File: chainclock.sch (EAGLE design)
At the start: 11 parts

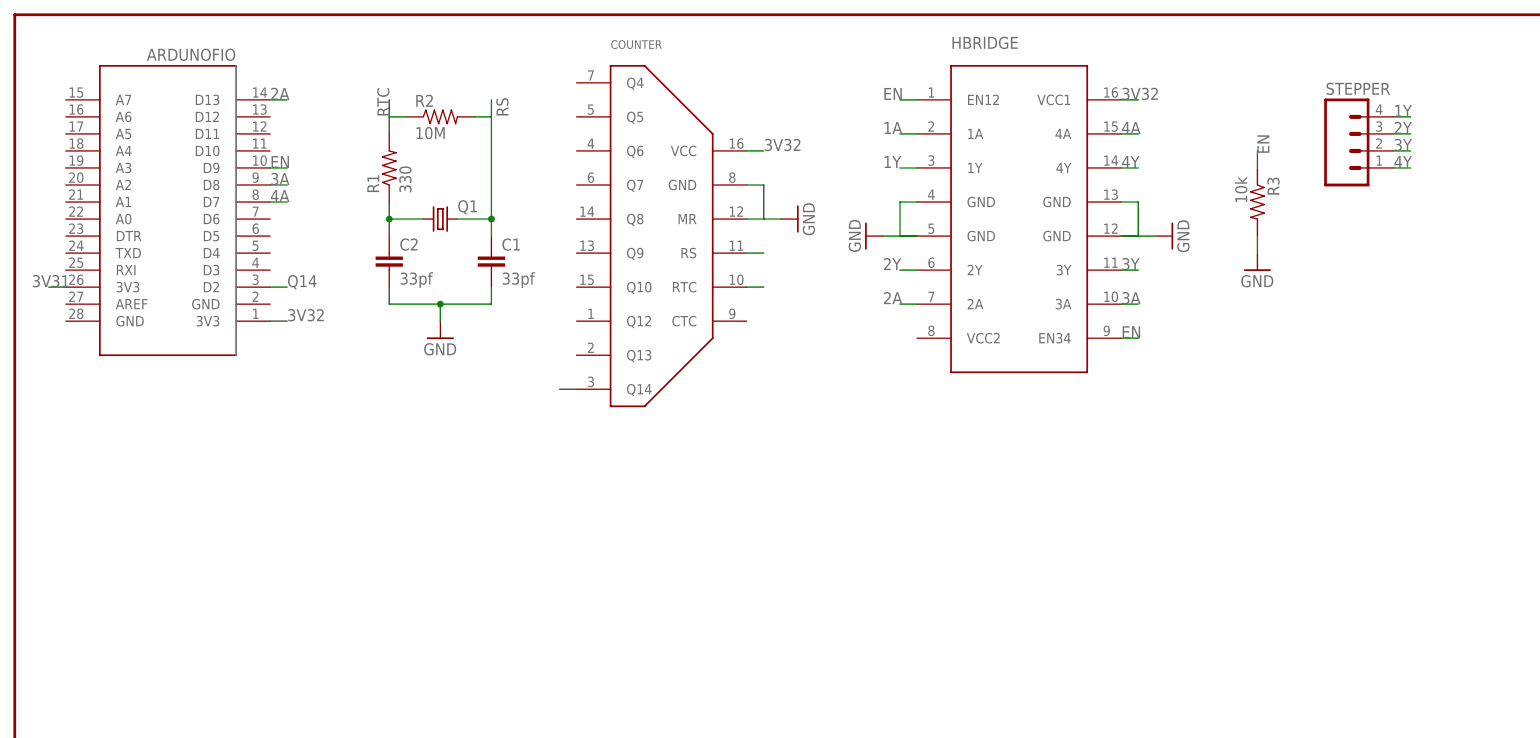
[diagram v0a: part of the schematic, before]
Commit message: Updates to chainclock, adding motor
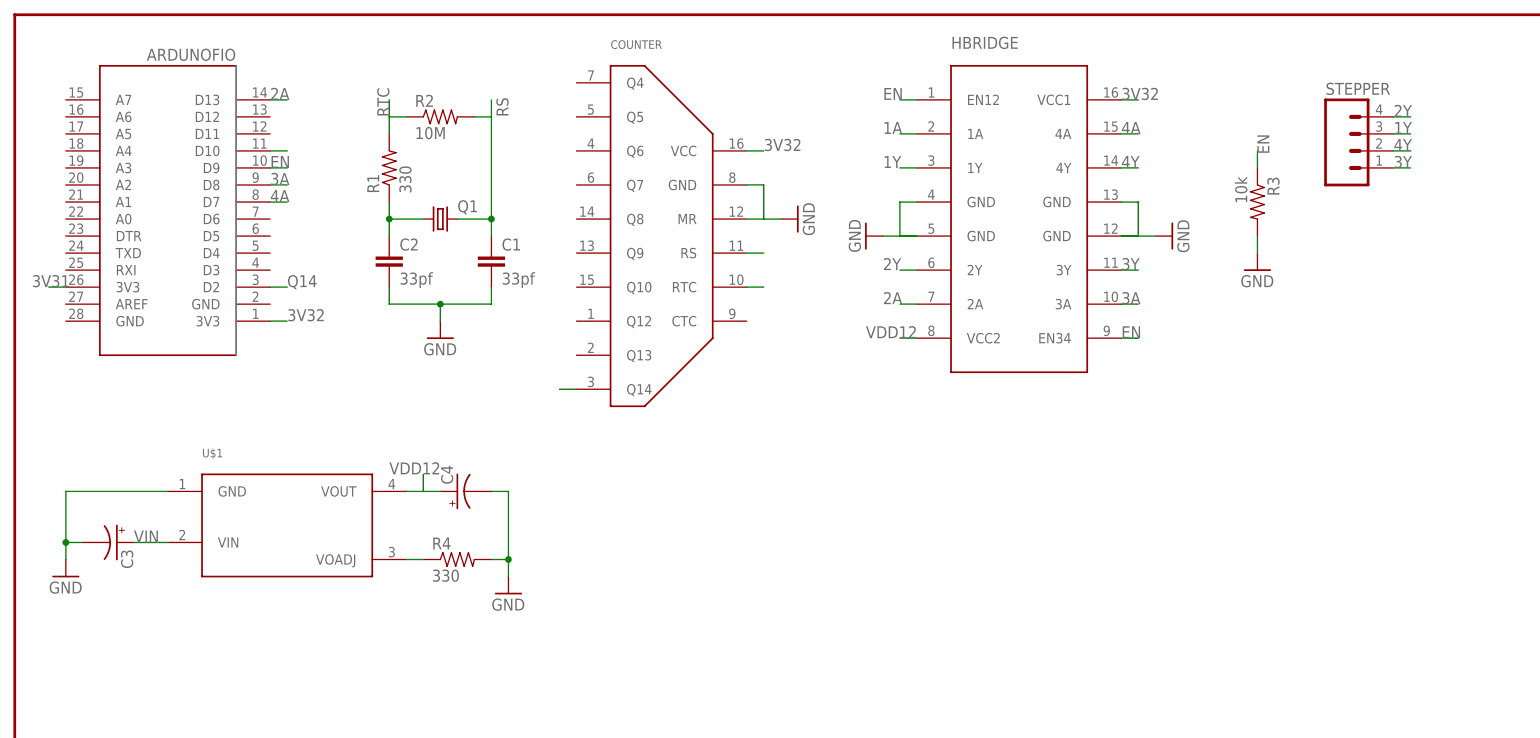
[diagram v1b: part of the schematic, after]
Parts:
- added C3, C4: (no value), SparkFun-Passives:CAP_POLPTH1
- added R4: 330, SparkFun-Resistors:RESISTOREZ
- added U$1: PTN0405C, desjardins:PTN0405C
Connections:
- new net N$3: R4.1, U$1.VOADJ
- new net VDD12: C4.+, HBRIDGE.VCC2, U$1.VOUT
- new net VIN: C3.+, U$1.VIN
- net 1A: now also ARDUNOFIO.D10
- net 1Y: now also STEPPER.3; no longer STEPPER.4
- net 2Y: now also STEPPER.4; no longer STEPPER.3
- net 3Y: now also STEPPER.1; no longer STEPPER.2
- net 4Y: now also STEPPER.2; no longer STEPPER.1
- net GND: now also C3.-, C4.-, R4.2, U$1.GND
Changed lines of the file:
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@@
 <layer number="97" name="Info" color="7" fill="1" visible="yes" active="yes"/>
 <layer number="98" name="Guide" color="6" fill="1" visible="yes" active="yes"/>
+<layer number="99" name="SpiceOrder" color="5" fill="1" visible="yes" active="yes"/>
 <layer number="100" name="Muster" color="7" fill="1" visible="no" active="no"/>
 <layer number="101" name="Patch_Top" color="12" fill="4" visible="yes" active="yes"/>
@@
 <part name="R3" library="SparkFun-Resistors" deviceset="RESISTOR" device="EZ" value="10k"/>
 <part name="GND5" library="SparkFun-Aesthetics" deviceset="GND" device=""/>
+<part name="U$1" library="desjardins" deviceset="PTN0405C" device=""/>
+<part name="C3" library="SparkFun-Passives" deviceset="CAP_POL" device="PTH1"/>
+<part name="C4" library="SparkFun-Passives" deviceset="CAP_POL" device="PTH1"/>
+<part name="GND6" library="SparkFun-Aesthetics" deviceset="GND" device=""/>
+<part name="R4" library="SparkFun-Resistors" deviceset="RESISTOR" device="EZ" value="330"/>
+<part name="GND8" library="SparkFun-Aesthetics" deviceset="GND" device=""/>
 </parts>
 <sheets>
@@
 <instance part="R3" gate="G$1" x="185.42" y="157.48" rot="R270"/>
 <instance part="GND5" gate="1" x="185.42" y="147.32"/>
+<instance part="U$1" gate="G$1" x="40.64" y="109.22"/>
+<instance part="C3" gate="G$1" x="15.24" y="106.68" rot="R270"/>
+<instance part="C4" gate="G$1" x="66.04" y="114.3" rot="R90"/>
+<instance part="GND6" gate="1" x="7.62" y="101.6"/>
+<instance part="R4" gate="G$1" x="66.04" y="104.14"/>
+<instance part="GND8" gate="1" x="73.66" y="99.06"/>
 </instances>
 <busses>
@@
 <wire x1="185.42" y1="152.4" x2="185.42" y2="149.86" width="0.1524" layer="91"/>
 <pinref part="GND5" gate="1" pin="GND"/>
+</segment>
+<segment>
+<pinref part="U$1" gate="G$1" pin="GND"/>
+<wire x1="22.86" y1="114.3" x2="7.62" y2="114.3" width="0.1524" layer="91"/>
+<wire x1="7.62" y1="114.3" x2="7.62" y2="106.68" width="0.1524" layer="91"/>
+<pinref part="C3" gate="G$1" pin="-"/>
+<wire x1="7.62" y1="106.68" x2="7.62" y2="104.14" width="0.1524" layer="91"/>
+<wire x1="10.16" y1="106.68" x2="7.62" y2="106.68" width="0.1524" layer="91"/>
+<junction x="7.62" y="106.68"/>
+<pinref part="GND6" gate="1" pin="GND"/>
+</segment>
+<segment>
+<pinref part="R4" gate="G$1" pin="2"/>
+<wire x1="71.12" y1="104.14" x2="73.66" y2="104.14" width="0.1524" layer="91"/>
+<wire x1="73.66" y1="104.14" x2="73.66" y2="101.6" width="0.1524" layer="91"/>
+<pinref part="GND8" gate="1" pin="GND"/>
+<pinref part="C4" gate="G$1" pin="-"/>
+<wire x1="71.12" y1="114.3" x2="73.66" y2="114.3" width="0.1524" layer="91"/>
+<wire x1="73.66" y1="114.3" x2="73.66" y2="104.14" width="0.1524" layer="91"/>
+<junction x="73.66" y="104.14"/>
 </segment>
 </net>
@@
 <label x="129.54" y="167.64" size="1.778" layer="95"/>
 </segment>
+<segment>
+<pinref part="ARDUNOFIO" gate="G$1" pin="D10"/>
+<wire x1="38.1" y1="165.1" x2="40.64" y2="165.1" width="0.1524" layer="91"/>
+</segment>
 </net>
 <net name="1Y" class="0">
@@
 </segment>
 <segment>
+<pinref part="STEPPER" gate="G$1" pin="3"/>
+<wire x1="205.74" y1="167.64" x2="208.28" y2="167.64" width="0.1524" layer="91"/>
+<label x="205.74" y="167.64" size="1.778" layer="95"/>
+</segment>
+</net>
+<net name="4A" class="0">
+<segment>
+<pinref part="HBRIDGE" gate="G$1" pin="4A"/>
+<wire x1="165.1" y1="167.64" x2="167.64" y2="167.64" width="0.1524" layer="91"/>
+<label x="165.1" y="167.64" size="1.778" layer="95"/>
+</segment>
+<segment>
+<pinref part="ARDUNOFIO" gate="G$1" pin="D7"/>
+<wire x1="38.1" y1="157.48" x2="40.64" y2="157.48" width="0.1524" layer="91"/>
+<label x="38.1" y="157.48" size="1.778" layer="95"/>
+</segment>
+</net>
+<net name="4Y" class="0">
+<segment>
+<pinref part="HBRIDGE" gate="G$1" pin="4Y"/>
+<wire x1="165.1" y1="162.56" x2="167.64" y2="162.56" width="0.1524" layer="91"/>
+<label x="165.1" y="162.56" size="1.778" layer="95"/>
+</segment>
+<segment>
+<pinref part="STEPPER" gate="G$1" pin="2"/>
+<wire x1="205.74" y1="165.1" x2="208.28" y2="165.1" width="0.1524" layer="91"/>
+<label x="205.74" y="165.1" size="1.778" layer="95"/>
+</segment>
+</net>
+<net name="3Y" class="0">
+<segment>
+<pinref part="HBRIDGE" gate="G$1" pin="3Y"/>
+<wire x1="165.1" y1="147.32" x2="167.64" y2="147.32" width="0.1524" layer="91"/>
+<label x="165.1" y="147.32" size="1.778" layer="95"/>
+</segment>
+<segment>
+<pinref part="STEPPER" gate="G$1" pin="1"/>
+<wire x1="205.74" y1="162.56" x2="208.28" y2="162.56" width="0.1524" layer="91"/>
+<label x="205.74" y="162.56" size="1.778" layer="95"/>
+</segment>
+</net>
+<net name="3A" class="0">
+<segment>
+<pinref part="HBRIDGE" gate="G$1" pin="3A"/>
+<wire x1="165.1" y1="142.24" x2="167.64" y2="142.24" width="0.1524" layer="91"/>
+<label x="165.1" y="142.24" size="1.778" layer="95"/>
+</segment>
+<segment>
+<pinref part="ARDUNOFIO" gate="G$1" pin="D8"/>
+<wire x1="38.1" y1="160.02" x2="40.64" y2="160.02" width="0.1524" layer="91"/>
+<label x="38.1" y="160.02" size="1.778" layer="95"/>
+</segment>
+</net>
+<net name="2A" class="0">
+<segment>
+<pinref part="HBRIDGE" gate="G$1" pin="2A"/>
+<wire x1="134.62" y1="142.24" x2="132.08" y2="142.24" width="0.1524" layer="91"/>
+<label x="129.54" y="142.24" size="1.778" layer="95"/>
+</segment>
+<segment>
+<pinref part="ARDUNOFIO" gate="G$1" pin="D13"/>
+<wire x1="38.1" y1="172.72" x2="40.64" y2="172.72" width="0.1524" layer="91"/>
+<label x="38.1" y="172.72" size="1.778" layer="95"/>
+</segment>
+</net>
+<net name="2Y" class="0">
+<segment>
+<pinref part="HBRIDGE" gate="G$1" pin="2Y"/>
+<wire x1="134.62" y1="147.32" x2="132.08" y2="147.32" width="0.1524" layer="91"/>
+<label x="129.54" y="147.32" size="1.778" layer="95"/>
+</segment>
+<segment>
 <pinref part="STEPPER" gate="G$1" pin="4"/>
 <wire x1="205.74" y1="170.18" x2="208.28" y2="170.18" width="0.1524" layer="91"/>
@@
 </segment>
 </net>
-<net name="4A" class="0">
-<segment>
-<pinref part="HBRIDGE" gate="G$1" pin="4A"/>
-<wire x1="165.1" y1="167.64" x2="167.64" y2="167.64" width="0.1524" layer="91"/>
-<label x="165.1" y="167.64" size="1.778" layer="95"/>
-</segment>
-<segment>
-<pinref part="ARDUNOFIO" gate="G$1" pin="D7"/>
-<wire x1="38.1" y1="157.48" x2="40.64" y2="157.48" width="0.1524" layer="91"/>
-<label x="38.1" y="157.48" size="1.778" layer="95"/>
-</segment>
-</net>
-<net name="4Y" class="0">
-<segment>
-<pinref part="HBRIDGE" gate="G$1" pin="4Y"/>
-<wire x1="165.1" y1="162.56" x2="167.64" y2="162.56" width="0.1524" layer="91"/>
-<label x="165.1" y="162.56" size="1.778" layer="95"/>
-</segment>
-<segment>
-<pinref part="STEPPER" gate="G$1" pin="1"/>
-<wire x1="205.74" y1="162.56" x2="208.28" y2="162.56" width="0.1524" layer="91"/>
-<label x="205.74" y="162.56" size="1.778" layer="95"/>
-</segment>
-</net>
-<net name="3Y" class="0">
-<segment>
-<pinref part="HBRIDGE" gate="G$1" pin="3Y"/>
-<wire x1="165.1" y1="147.32" x2="167.64" y2="147.32" width="0.1524" layer="91"/>
-<label x="165.1" y="147.32" size="1.778" layer="95"/>
-</segment>
-<segment>
-<pinref part="STEPPER" gate="G$1" pin="2"/>
-<wire x1="205.74" y1="165.1" x2="208.28" y2="165.1" width="0.1524" layer="91"/>
-<label x="205.74" y="165.1" size="1.778" layer="95"/>
-</segment>
-</net>
-<net name="3A" class="0">
-<segment>
-<pinref part="HBRIDGE" gate="G$1" pin="3A"/>
-<wire x1="165.1" y1="142.24" x2="167.64" y2="142.24" width="0.1524" layer="91"/>
-<label x="165.1" y="142.24" size="1.778" layer="95"/>
-</segment>
-<segment>
-<pinref part="ARDUNOFIO" gate="G$1" pin="D8"/>
-<wire x1="38.1" y1="160.02" x2="40.64" y2="160.02" width="0.1524" layer="91"/>
-<label x="38.1" y="160.02" size="1.778" layer="95"/>
-</segment>
-</net>
-<net name="2A" class="0">
-<segment>
-<pinref part="HBRIDGE" gate="G$1" pin="2A"/>
-<wire x1="134.62" y1="142.24" x2="132.08" y2="142.24" width="0.1524" layer="91"/>
-<label x="129.54" y="142.24" size="1.778" layer="95"/>
-</segment>
-<segment>
-<pinref part="ARDUNOFIO" gate="G$1" pin="D13"/>
-<wire x1="38.1" y1="172.72" x2="40.64" y2="172.72" width="0.1524" layer="91"/>
-<label x="38.1" y="172.72" size="1.778" layer="95"/>
-</segment>
-</net>
-<net name="2Y" class="0">
-<segment>
-<pinref part="HBRIDGE" gate="G$1" pin="2Y"/>
-<wire x1="134.62" y1="147.32" x2="132.08" y2="147.32" width="0.1524" layer="91"/>
-<label x="129.54" y="147.32" size="1.778" layer="95"/>
-</segment>
-<segment>
-<pinref part="STEPPER" gate="G$1" pin="3"/>
-<wire x1="205.74" y1="167.64" x2="208.28" y2="167.64" width="0.1524" layer="91"/>
-<label x="205.74" y="167.64" size="1.778" layer="95"/>
-</segment>
-</net>
 <net name="3V31" class="0">
 <segment>
@@
 </segment>
 </net>
+<net name="VIN" class="0">
+<segment>
+<pinref part="U$1" gate="G$1" pin="VIN"/>
+<label x="17.78" y="106.68" size="1.778" layer="95"/>
+<pinref part="C3" gate="G$1" pin="+"/>
+<wire x1="22.86" y1="106.68" x2="17.78" y2="106.68" width="0.1524" layer="91"/>
+</segment>
+</net>
+<net name="VDD12" class="0">
+<segment>
+<pinref part="U$1" gate="G$1" pin="VOUT"/>
+<wire x1="58.42" y1="114.3" x2="60.96" y2="114.3" width="0.1524" layer="91"/>
+<pinref part="C4" gate="G$1" pin="+"/>
+<wire x1="60.96" y1="114.3" x2="63.5" y2="114.3" width="0.1524" layer="91"/>
+<wire x1="60.96" y1="114.3" x2="60.96" y2="116.84" width="0.1524" layer="91"/>
+<label x="55.88" y="116.84" size="1.778" layer="95"/>
+</segment>
+<segment>
+<pinref part="HBRIDGE" gate="G$1" pin="VCC2"/>
+<wire x1="134.62" y1="137.16" x2="132.08" y2="137.16" width="0.1524" layer="91"/>
+<label x="127" y="137.16" size="1.778" layer="95"/>
+</segment>
+</net>
+<net name="N$3" class="0">
+<segment>
+<pinref part="U$1" gate="G$1" pin="VOADJ"/>
+<wire x1="58.42" y1="104.14" x2="60.96" y2="104.14" width="0.1524" layer="91"/>
+<pinref part="R4" gate="G$1" pin="1"/>
+</segment>
+</net>

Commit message: Move some stuff around
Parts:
- removed FRAME1: FRAME-LETTER, SparkFun-Aesthetics:FRAME-LETTER
- R4: value 330 -> 1.35k
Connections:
- net 1Y: now also STEPPER.4; no longer STEPPER.3
- net 2Y: now also STEPPER.3; no longer STEPPER.4
- net 3Y: now also STEPPER.2; no longer STEPPER.1
- net 4Y: now also STEPPER.1; no longer STEPPER.2
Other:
- moved on the sheet: ARDUNOFIO, C1, C2, C3, C4, COUNTER, HBRIDGE, Q1, R1, R2, R3, R4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
